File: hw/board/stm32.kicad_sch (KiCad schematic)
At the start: 0 parts

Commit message: Added reset + boot switches for STM32, re-routed power
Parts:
- added R10, R5, R8, R9: 4k7, Resistor_SMD:R_0805_2012Metric, symbol Device:R
- added R6: 330, Resistor_SMD:R_0805_2012Metric, symbol Device:R
- added SW1, SW2: TSB008A2526A, EasyEDA:SW-SMD_L6.0-W3.5-LS8.0, symbol EasyEDA:TSB008A2526A
- added U5: STM32F302CBTx, Package_QFP:LQFP-48_7x7mm_P0.5mm, symbol MCU_ST_STM32F3:STM32F302CBTx
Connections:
- new net: R10.1, SW1.1, U5.44 (BOOT0)
- new net: R9.2, SW2.2, U5.7 (NRST)
- new net +2V5: R5.1, R6.1, R8.1, R9.1, SW1.2, U5.1 (VBAT), U5.24 (VDD), U5.36 (VDD), U5.48 (VDD), U5.9 (VDDA)
- new net CCLK: U5.15 (PA5)
- new net DIN: U5.17 (PA7)
- new net DONE: R6.2, U5.10 (PA0)
- new net FLASH_MISO: U5.27 (PB14)
- new net FLASH_MOSI: U5.28 (PB15)
- new net FLASH_SCK: U5.26 (PB13)
- new net GND: R10.2, SW2.1, U5.23 (VSS), U5.35 (VSS), U5.47 (VSS), U5.8 (VSSA)
- new net INIT_B: R5.2, U5.12 (PA2)
- new net PROGRAM_B: R8.2, U5.11 (PA1)
- new net USB_D_N: U5.32 (PA11)
- new net USB_D_P: U5.33 (PA12)
- new net ~{FLASH_CS}: U5.25 (PB12)
- no-connect marks 0 -> 26

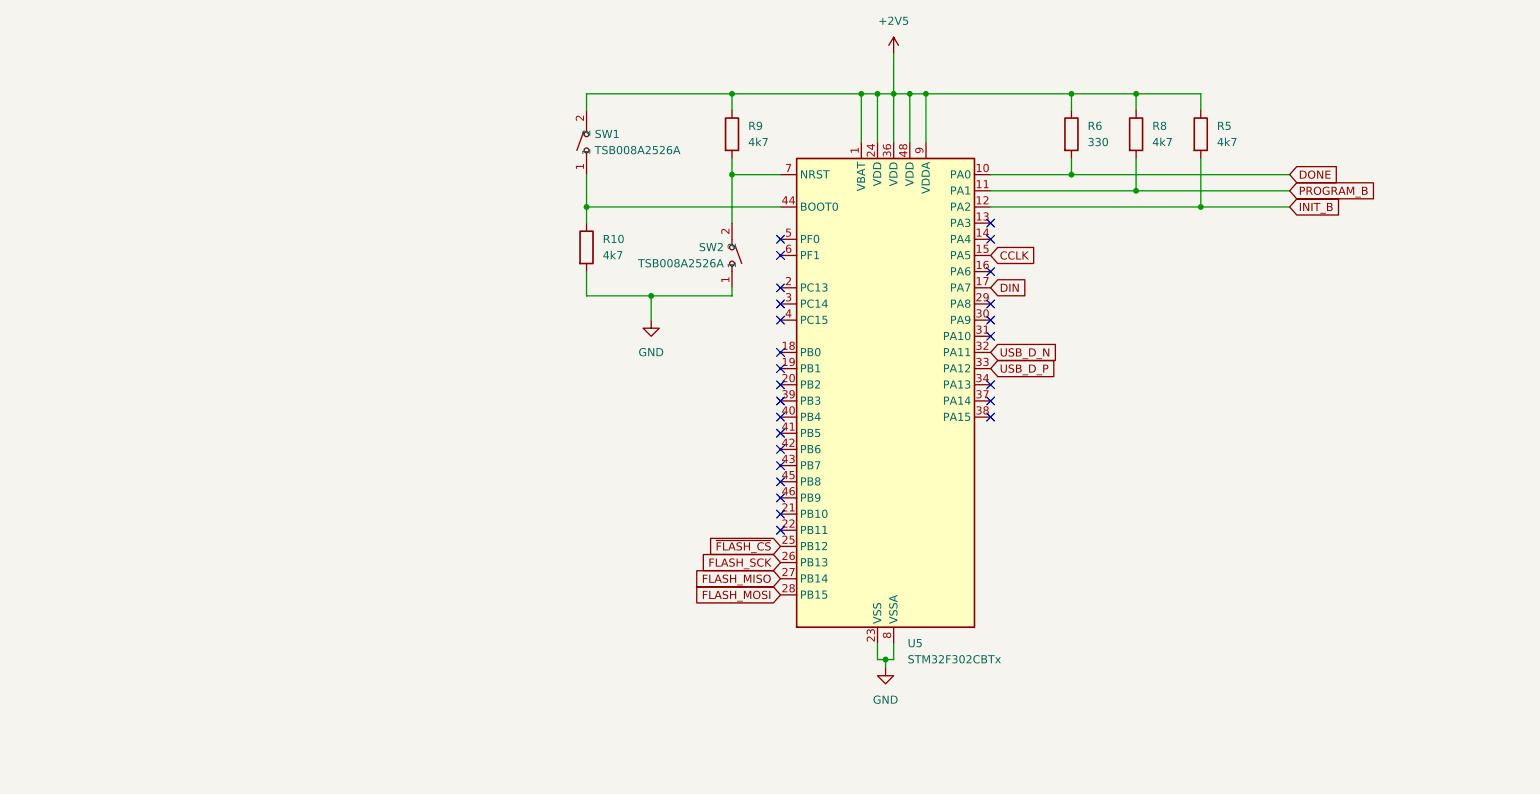
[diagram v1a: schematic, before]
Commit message: Added power connector, SWD/JTAG connectors
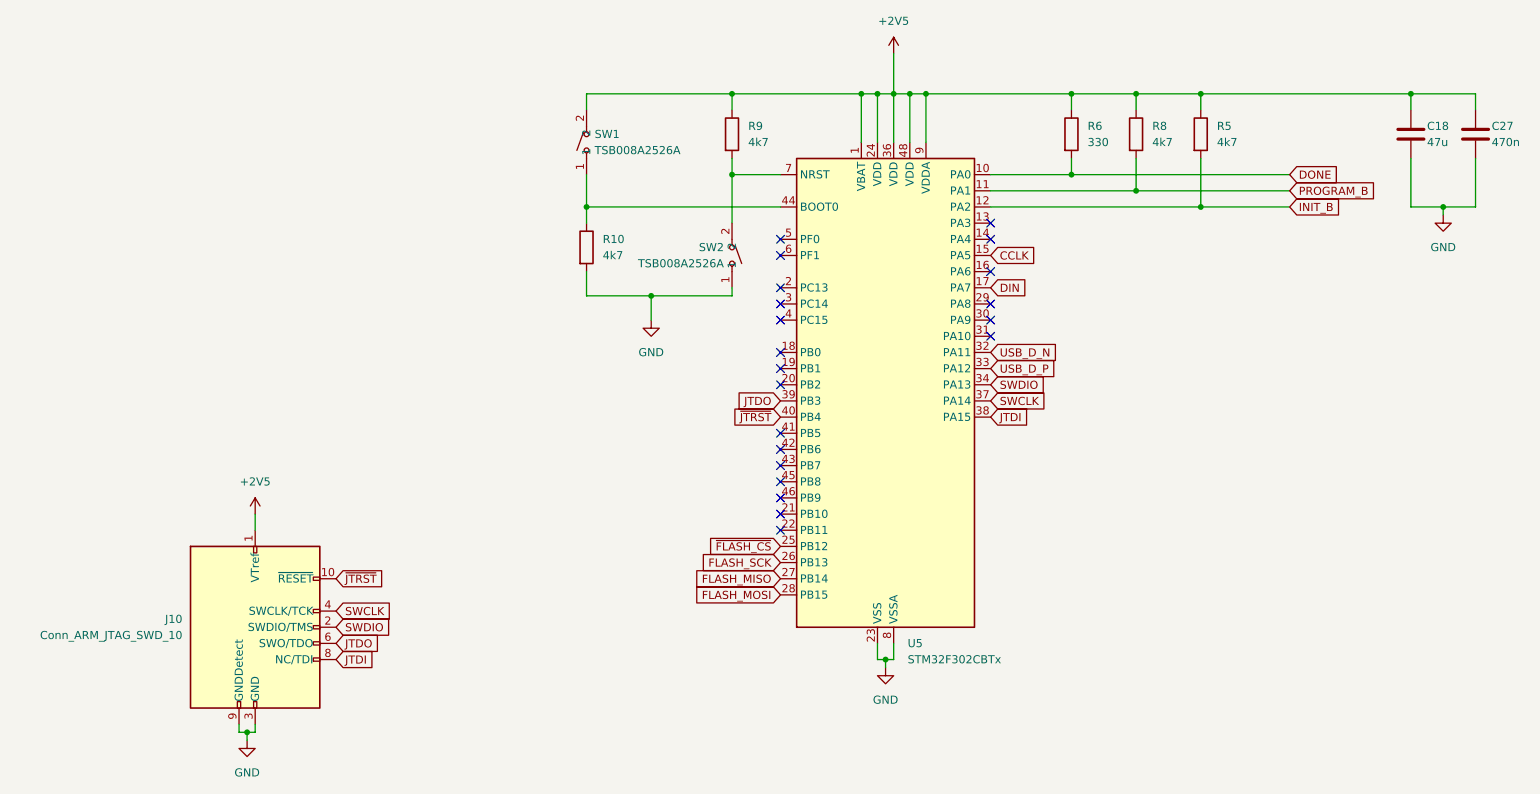
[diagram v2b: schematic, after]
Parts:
- added C18: 47u, Capacitor_SMD:C_0805_2012Metric, symbol Device:C
- added C27: 470n, Capacitor_SMD:C_0805_2012Metric, symbol Device:C
- added J10: Conn_ARM_JTAG_SWD_10, Connector_PinHeader_1.27mm:PinHeader_2x05_P1.27mm_Vertical, symbol Connector:Conn_ARM_JTAG_SWD_10
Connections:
- net +2V5: now also C18.1, C27.1, J10.1 (VTref)
- net GND: now also C18.2, C27.2, J10.3 (GND), J10.5 (GND), J10.9 (GNDDetect)
- net SWDIO: now reaches U5.34 (PA13)
- net SWDIO: now also J10.2 (SWDIO/TMS)
- net SWCLK: now reaches U5.37 (PA14)
- net SWCLK: now also J10.4 (SWCLK/TCK)
- net JTDI: now reaches U5.38 (PA15)
- net JTDI: now also J10.8 (NC/TDI)
- net JTDO: now reaches U5.39 (PB3)
- net JTDO: now also J10.6 (SWO/TDO)
- net ~{JTRST}: now reaches U5.40 (PB4)
- net ~{JTRST}: now also J10.10 (~{RESET})
- no-connect marks 26 -> 21

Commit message: Reannotated piece numbers
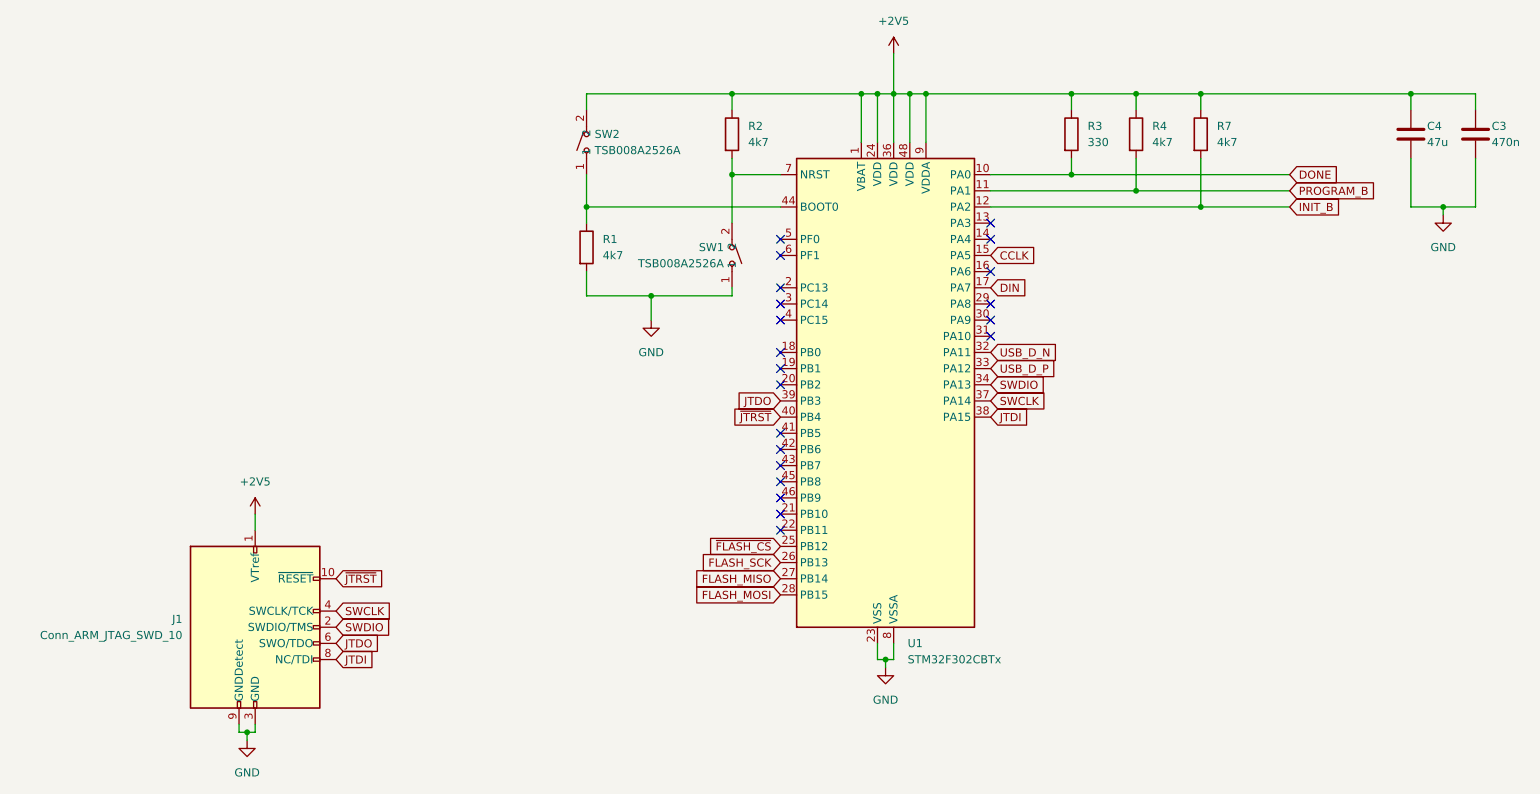
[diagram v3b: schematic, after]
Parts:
- renumbered C27 to C3, C18 to C4, J10 to J1, R10 to R1, R9 to R2, R6 to R3, R8 to R4, R5 to R7, SW2 to SW1, SW1 to SW2, U5 to U1
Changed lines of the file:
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@@
 		(dnp no)
 		(fields_autoplaced yes)
-		(property "Reference" "U5"
+		(property "Reference" "U1"
 			(at 144.4341 127 0)
 			(effects
@@
 			(project "board"
 				(path "/0e384709-6bce-4dbf-a0e0-550e970390f4/1f74052e-5889-441a-be42-0e37c50cc8ab"
-					(reference "U5")
+					(reference "U1")
 					(unit 1)
 				)
@@
 		(dnp no)
 		(fields_autoplaced yes)
-		(property "Reference" "J10"
+		(property "Reference" "J1"
 			(at 30.48 123.1899 0)
 			(effects
@@
 			(project "board"
 				(path "/0e384709-6bce-4dbf-a0e0-550e970390f4/1f74052e-5889-441a-be42-0e37c50cc8ab"
-					(reference "J10")
+					(reference "J1")
 					(unit 1)
 				)
@@
 		(dnp no)
 		(fields_autoplaced yes)
-		(property "Reference" "R10"
+		(property "Reference" "R1"
 			(at 96.52 63.4999 0)
 			(effects
@@
 			(project "board"
 				(path "/0e384709-6bce-4dbf-a0e0-550e970390f4/1f74052e-5889-441a-be42-0e37c50cc8ab"
-					(reference "R10")
+					(reference "R1")
 					(unit 1)
 				)
@@
 		(dnp no)
 		(fields_autoplaced yes)
-		(property "Reference" "SW1"
+		(property "Reference" "SW2"
 			(at 95.25 46.9899 90)
 			(effects
@@
 			(project ""
 				(path "/0e384709-6bce-4dbf-a0e0-550e970390f4/1f74052e-5889-441a-be42-0e37c50cc8ab"
-					(reference "SW1")
+					(reference "SW2")
 					(unit 1)
 				)
@@
 		(dnp no)
 		(fields_autoplaced yes)
-		(property "Reference" "R9"
+		(property "Reference" "R2"
 			(at 119.38 45.7199 0)
 			(effects
@@
 			(project "board"
 				(path "/0e384709-6bce-4dbf-a0e0-550e970390f4/1f74052e-5889-441a-be42-0e37c50cc8ab"
-					(reference "R9")
+					(reference "R2")
 					(unit 1)
 				)
@@
 		(on_board yes)
 		(dnp no)
-		(property "Reference" "C18"
+		(property "Reference" "C4"
 			(at 226.06 45.72 0)
 			(effects
@@
 			(project "board"
 				(path "/0e384709-6bce-4dbf-a0e0-550e970390f4/1f74052e-5889-441a-be42-0e37c50cc8ab"
-					(reference "C18")
+					(reference "C4")
 					(unit 1)
 				)
@@
 		(on_board yes)
 		(dnp no)
-		(property "Reference" "SW2"
+		(property "Reference" "SW1"
 			(at 115.57 64.7699 90)
 			(effects
@@
 			(project "board"
 				(path "/0e384709-6bce-4dbf-a0e0-550e970390f4/1f74052e-5889-441a-be42-0e37c50cc8ab"
-					(reference "SW2")
+					(reference "SW1")
 					(unit 1)
 				)
@@
 		(dnp no)
 		(fields_autoplaced yes)
-		(property "Reference" "R8"
+		(property "Reference" "R4"
 			(at 182.88 45.7199 0)
 			(effects
@@
 			(project "board"
 				(path "/0e384709-6bce-4dbf-a0e0-550e970390f4/1f74052e-5889-441a-be42-0e37c50cc8ab"
-					(reference "R8")
+					(reference "R4")
 					(unit 1)
 				)
@@
 		(on_board yes)
 		(dnp no)
-		(property "Reference" "C27"
+		(property "Reference" "C3"
 			(at 236.22 45.72 0)
 			(effects
@@
 			(project "board"
 				(path "/0e384709-6bce-4dbf-a0e0-550e970390f4/1f74052e-5889-441a-be42-0e37c50cc8ab"
-					(reference "C27")
+					(reference "C3")
 					(unit 1)
 				)
@@
 		(dnp no)
 		(fields_autoplaced yes)
-		(property "Reference" "R6"
+		(property "Reference" "R3"
 			(at 172.72 45.7199 0)
 			(effects
@@
 			(project "board"
 				(path "/0e384709-6bce-4dbf-a0e0-550e970390f4/1f74052e-5889-441a-be42-0e37c50cc8ab"
-					(reference "R6")
+					(reference "R3")
 					(unit 1)
 				)
@@
 		(dnp no)
 		(fields_autoplaced yes)
-		(property "Reference" "R5"
+		(property "Reference" "R7"
 			(at 193.04 45.7199 0)
 			(effects
@@
 			(project "board"
 				(path "/0e384709-6bce-4dbf-a0e0-550e970390f4/1f74052e-5889-441a-be42-0e37c50cc8ab"
-					(reference "R5")
-					(unit 1)
-				)
+					(reference "R7")
+					(unit 1)
+				)

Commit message: Added capacitor for STM32 NRST
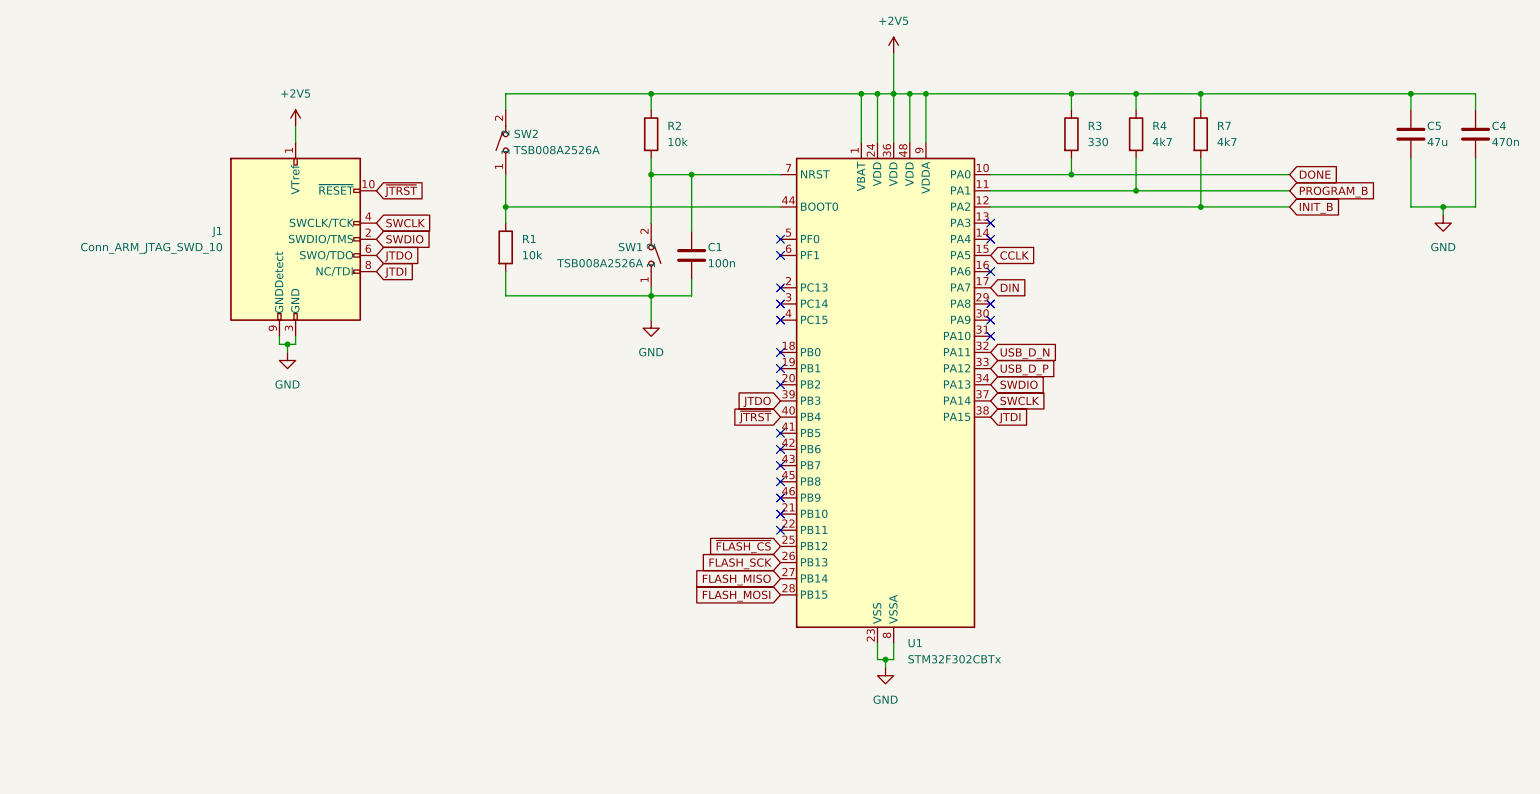
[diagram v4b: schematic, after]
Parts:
- added C1: 100n, Capacitor_SMD:C_0805_2012Metric, symbol Device:C
- R1, R2: value 4k7 -> 10k
- renumbered C3 to C4, C4 to C5
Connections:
- net GND: now also C1.2
- net at R2.2, SW1.2, U1.7 (NRST): now also C1.1
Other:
- moved on the sheet: J1, R1, R2, SW1, SW2
